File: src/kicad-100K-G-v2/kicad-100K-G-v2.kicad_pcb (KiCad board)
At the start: 2 copper layers, 35.6 x 47.6 mm, 29 parts, among them P1 In, P2 Out, P3 Power, U1 TL072

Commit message: corrections 2014-09-01
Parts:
- C5: value 10n -> 6.8n

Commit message: 28/09/2014 minor changes
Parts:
- R10: value 500 -> 470
- R2: value 5Meg -> 4.7Meg
- moved R1 0.64 mm to (116.8, 115.6)
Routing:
- net Net-(P1-Pad2): track 9.31 -> 8.67 mm
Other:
- board size 35.6 x 47.6 mm -> 35.6 x 48.3 mm

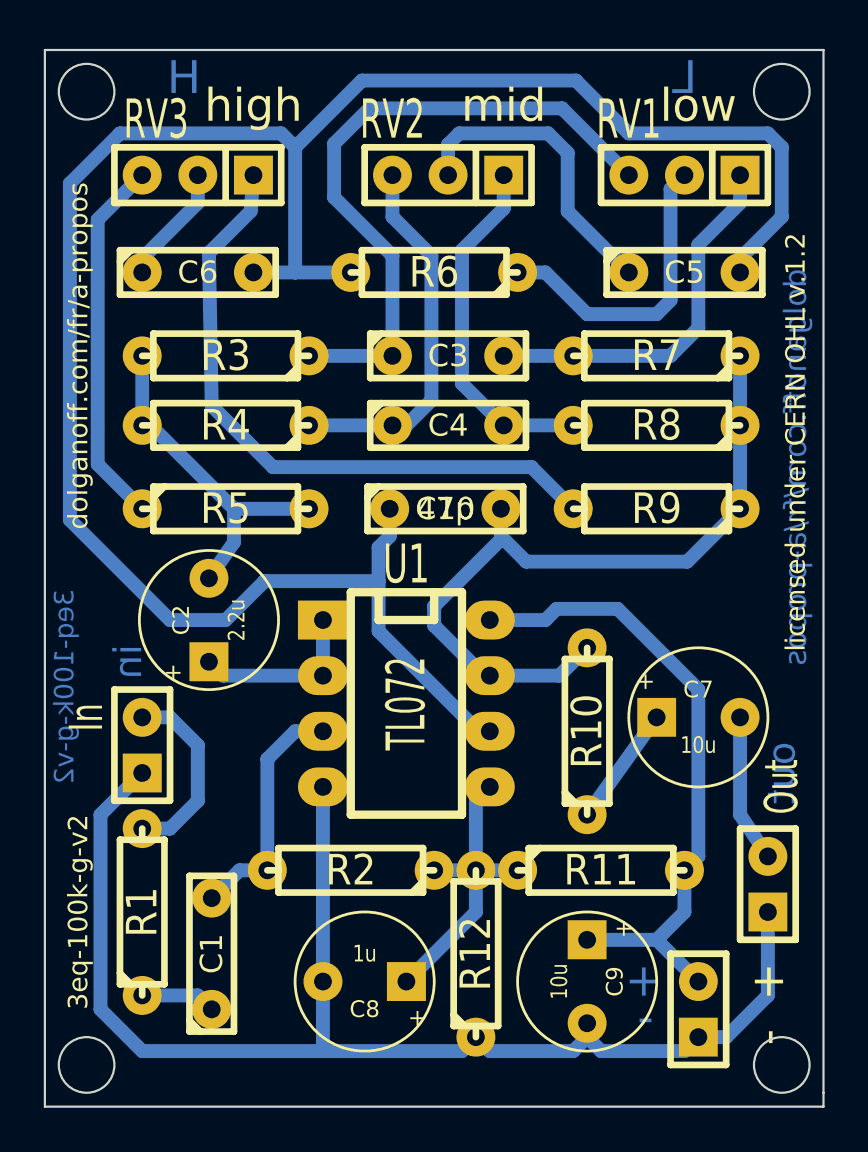
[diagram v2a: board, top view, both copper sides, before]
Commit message: 29/10/2014 corrections to 100K-G: version 2.1
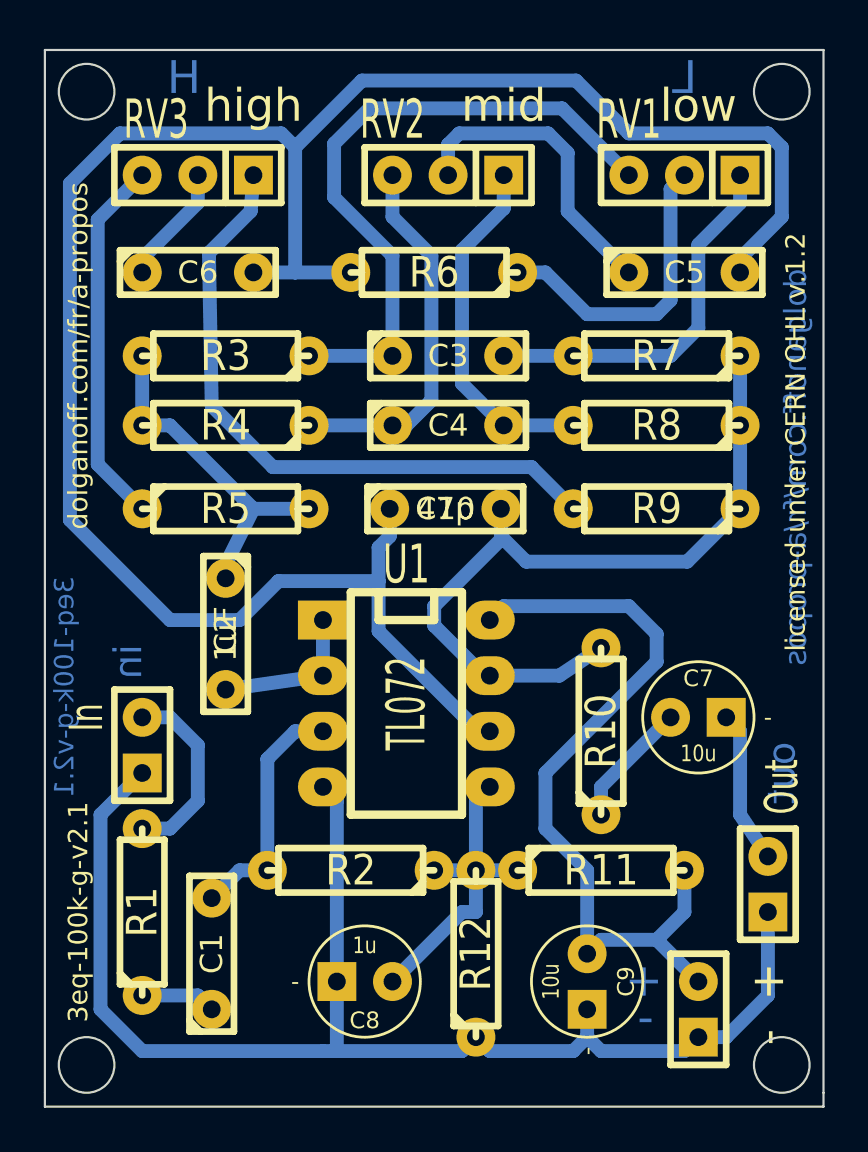
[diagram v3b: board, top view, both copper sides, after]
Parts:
- C2: value 2.2u -> 1uF; footprint Custom:C1.5V7-LARGE_PADS -> Custom:C2-LARGE_PADS
- C7, C8, C9: footprint Custom:C1.5V7-LARGE_PADS -> Custom:C1V5-LARGE_PADS
- moved C2 0.99 mm to (120.7, 102.9), turned to 270 degrees
- moved R10 0.63 mm to (137.8, 107.3)
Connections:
- R3 pad 2: Net-(C2-Pad2) -> Net-(C2-Pad1)
- R4 pad 2: Net-(C2-Pad2) -> Net-(C2-Pad1)
- R5 pad 2: Net-(C2-Pad2) -> Net-(C2-Pad1)
- U1 pad 1: Net-(C2-Pad1) -> Net-(C2-Pad2)
- U1 pad 2: Net-(C2-Pad1) -> Net-(C2-Pad2)
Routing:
- net Net-(C2-Pad2): track 15.9 -> 7.03 mm
- net Net-(C2-Pad1): track 8.01 -> 16.2 mm
- net v+: track 29.3 -> 35.7 mm
- net GND: track 61.5 -> 62.4 mm
- net vRef: track 14.3 -> 14.9 mm
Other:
- board text added: "3eq-100k-g-v2.1"
- board text removed: "3eq-100k-g-v2"
